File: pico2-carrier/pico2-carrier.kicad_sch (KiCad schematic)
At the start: 27 parts, among them IC1 TFDU4101-TT3, IC2 M95512-DWDW4TP_K, IC3 W25Q128JVSIM_TR, SW1 RUN, SW2 BUT_L, SW3 BUT_M, SW4 BUT_R, U1 Pico 2

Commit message: start work on PCB
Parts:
- IC1: footprint TFDU4101-TR3 -> SamacsysParts:TFDU4101-TR3
- IC2: footprint SOP65P640X120-8N -> SamacsysParts:SOP65P640X120-8N
- IC3: footprint SOIC127P790X216-8N -> SamacsysParts:SOIC127P790X216-8N
- R3: footprint (none) -> Resistor_SMD:R_0402_1005Metric
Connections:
- net ACCEL_INT1: now also U1.11 (GPIO8); no longer U1.10 (GPIO7)
- net BUT_L: now also U1.25 (GPIO19); no longer U1.29 (GPIO22)
- net BUT_M: now also U1.29 (GPIO22); no longer U1.31 (GPIO26_ADC0)
- net BUT_R: now also U1.31 (GPIO26_ADC0); no longer U1.32 (GPIO27_ADC1)
- net ~{ACCEL_CSB}: now also U1.10 (GPIO7); no longer U1.9 (GPIO6)
- net ~{BAT_CE}: now also U1.32 (GPIO27_ADC1); no longer U1.34 (GPIO28_ADC2)
- net ~{BAT_INT}: now also U1.34 (GPIO28_ADC2); no longer U1.25 (GPIO19)
- net ~{FLASH_CSB}: now also U1.9 (GPIO6); no longer U1.11 (GPIO8)
- net VSYS_IN: now reaches JP2.1 (A), U1.39 (VSYS)
- net 3V3_OUT: now reaches JP3.1 (A), U1.35 (ADC_VREF), U1.36 (3V3)
- net VBUS_OUT: now reaches JP1.1 (A), U1.40 (VBUS)
- no-connect marks 4 -> 5
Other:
- note added: "Ceramic"
- note added: "Current lim = 60mA"
- note added: "Tantalum/fast rise"
- moved on the sheet: JP1, JP2

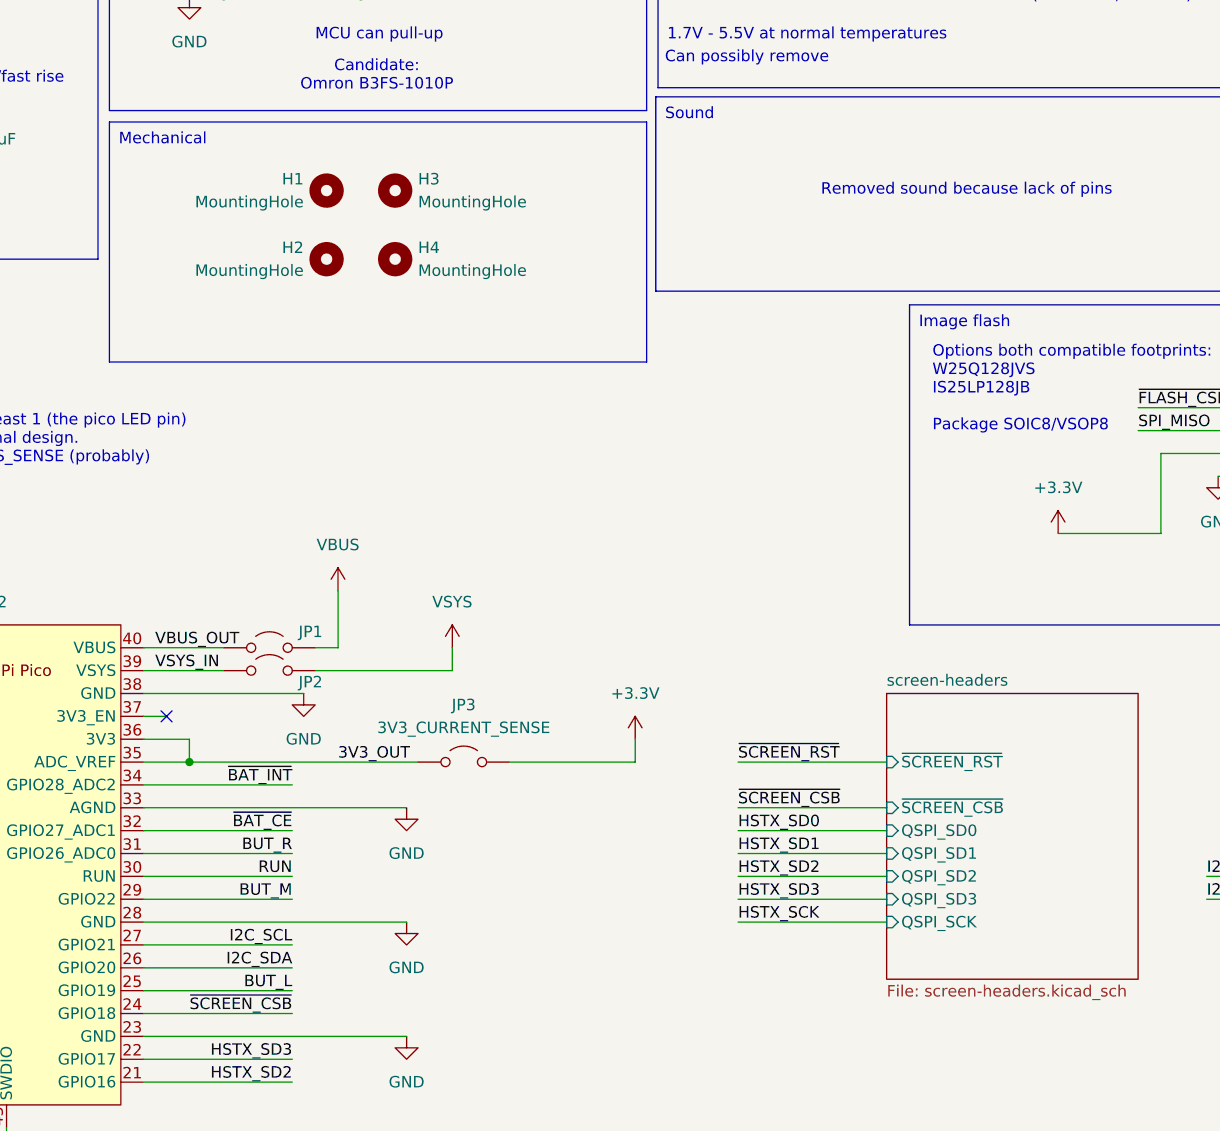
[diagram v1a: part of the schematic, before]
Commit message: finish routing - DRC ok
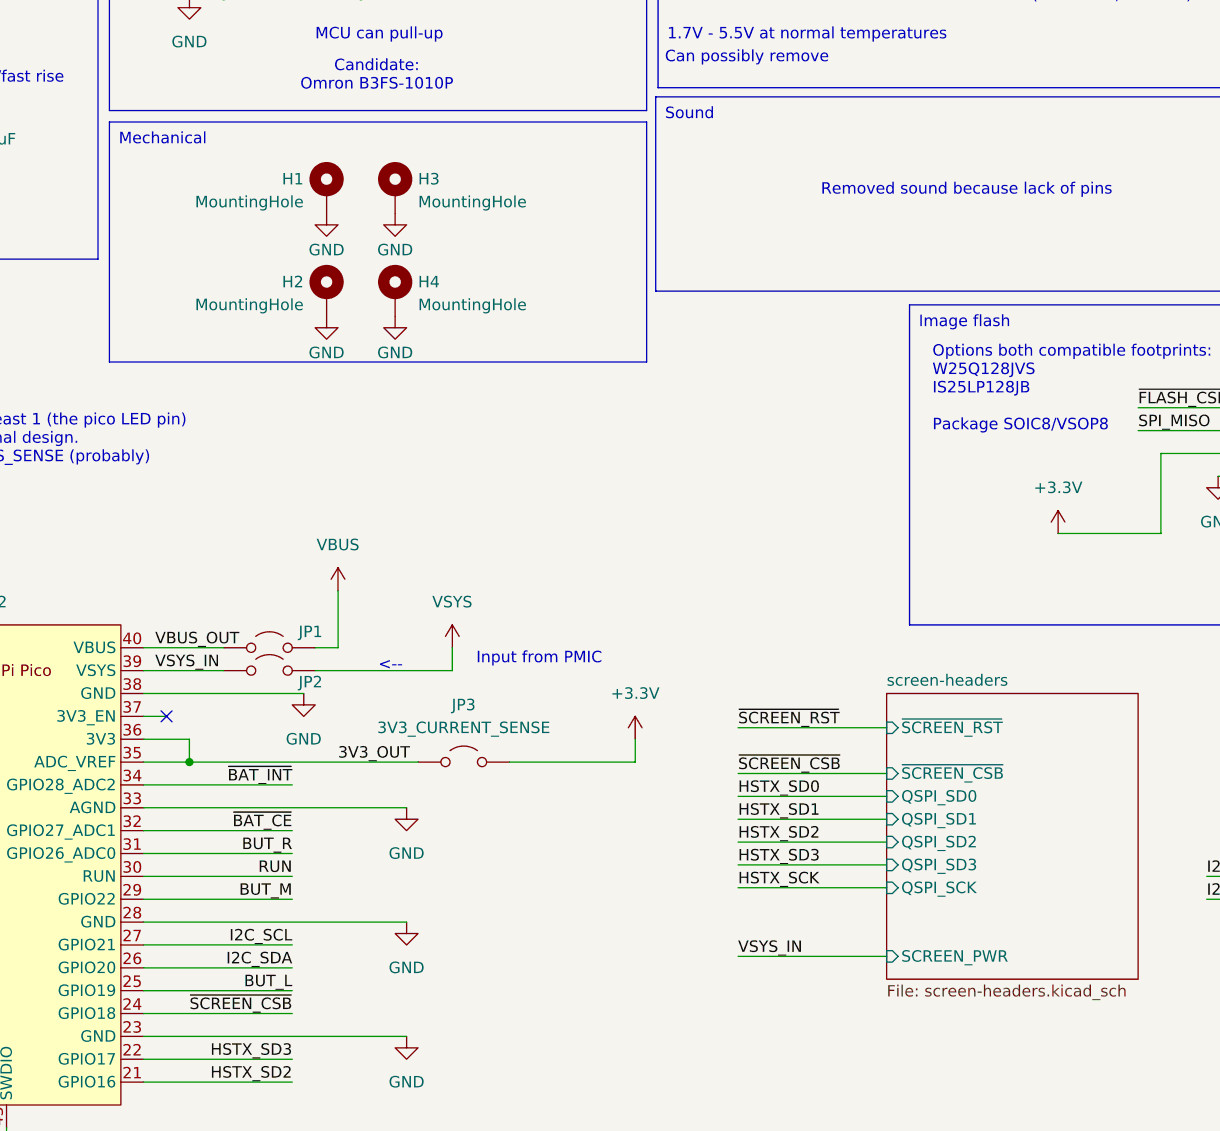
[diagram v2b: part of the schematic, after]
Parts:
- H1, H2, H3, H4: symbol Mechanical:MountingHole -> Mechanical:MountingHole_Pad
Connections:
- net GND: now also H1.1, H2.1, H3.1, H4.1
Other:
- sheet screen-headers ports: added SCREEN_PWR; removed none
- note added: "<--"
- note added: "Input from PMIC"

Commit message: pcb tweaks
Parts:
- H1, H2, H3, H4: footprint MountingHole:MountingHole_2.2mm_M2 -> MountingHole:MountingHole_2.2mm_M2_DIN965_Pad_TopBottom
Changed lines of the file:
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@@
 			)
 		)
-		(property "Footprint" "MountingHole:MountingHole_2.2mm_M2"
+		(property "Footprint" "MountingHole:MountingHole_2.2mm_M2_DIN965_Pad_TopBottom"
 			(at 115.57 76.2 0)
 			(effects
@@
 			)
 		)
-		(property "Footprint" "MountingHole:MountingHole_2.2mm_M2"
+		(property "Footprint" "MountingHole:MountingHole_2.2mm_M2_DIN965_Pad_TopBottom"
 			(at 107.95 64.77 0)
 			(effects
@@
 			)
 		)
-		(property "Footprint" "MountingHole:MountingHole_2.2mm_M2"
+		(property "Footprint" "MountingHole:MountingHole_2.2mm_M2_DIN965_Pad_TopBottom"
 			(at 107.95 76.2 0)
 			(effects
@@
 			)
 		)
-		(property "Footprint" "MountingHole:MountingHole_2.2mm_M2"
+		(property "Footprint" "MountingHole:MountingHole_2.2mm_M2_DIN965_Pad_TopBottom"
 			(at 115.57 64.77 0)
 			(effects

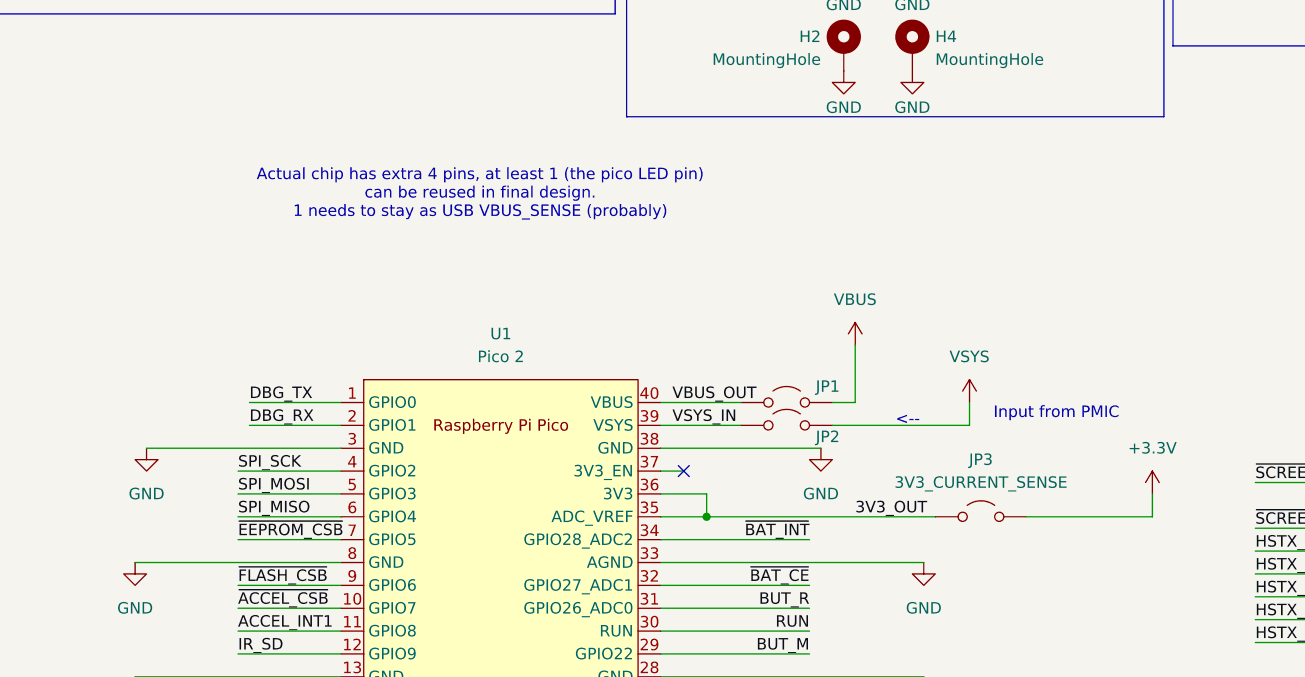
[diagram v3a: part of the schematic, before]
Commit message: add PFET to VSYS input
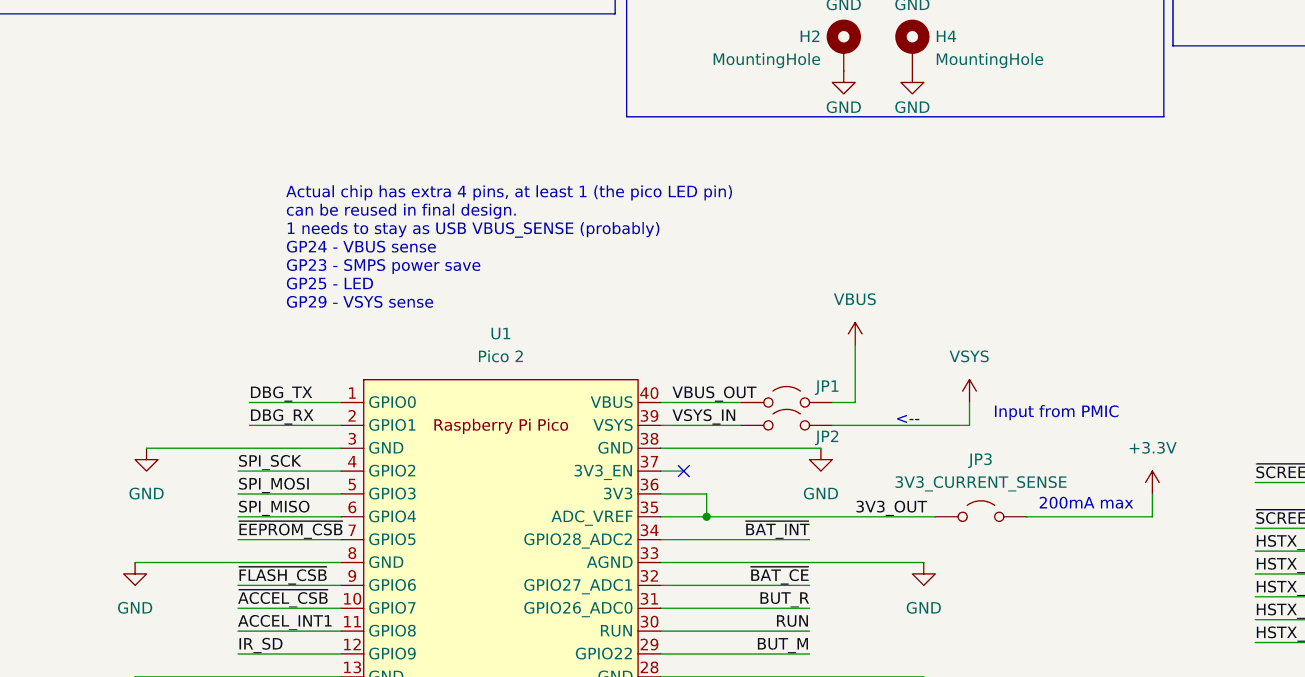
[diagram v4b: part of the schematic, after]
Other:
- note added: "200mA max"
- note added: "Actual chip has extra 4 pins, at least 1 (the pico LED pin) can be reused in final design. 1 needs to stay as USB VBUS_SENSE (probably) GP24 - VBUS sense GP23 - SMPS power save GP25 - LED GP29 - VSYS sense"
- note removed: "Actual chip has extra 4 pins, at least 1 (the pico LED pin) can be reused in final design. 1 needs to stay as USB VBUS_SENSE (probably)"
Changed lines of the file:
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@@
+		)
+	)
+	(text "200mA max"
+		(exclude_from_sim no)
+		(at 134.874 127 0)
+		(effects
+			(font
+				(size 1.27 1.27)
+			)
 		)
 	)
@@
 		)
 	)
-	(text "Actual chip has extra 4 pins, at least 1 (the pico LED pin)\ncan be reused in final design.\n1 needs to stay as USB VBUS_SENSE (probably)"
+	(text "Actual chip has extra 4 pins, at least 1 (the pico LED pin)\ncan be reused in final design.\n1 needs to stay as USB VBUS_SENSE (probably)\nGP24 - VBUS sense\nGP23 - SMPS power save\nGP25 - LED\nGP29 - VSYS sense"
 		(exclude_from_sim no)
-		(at 67.564 92.456 0)
+		(at 45.974 98.552 0)
 		(effects
 			(font
 				(size 1.27 1.27)
 			)
+			(justify left)
 		)
 	)

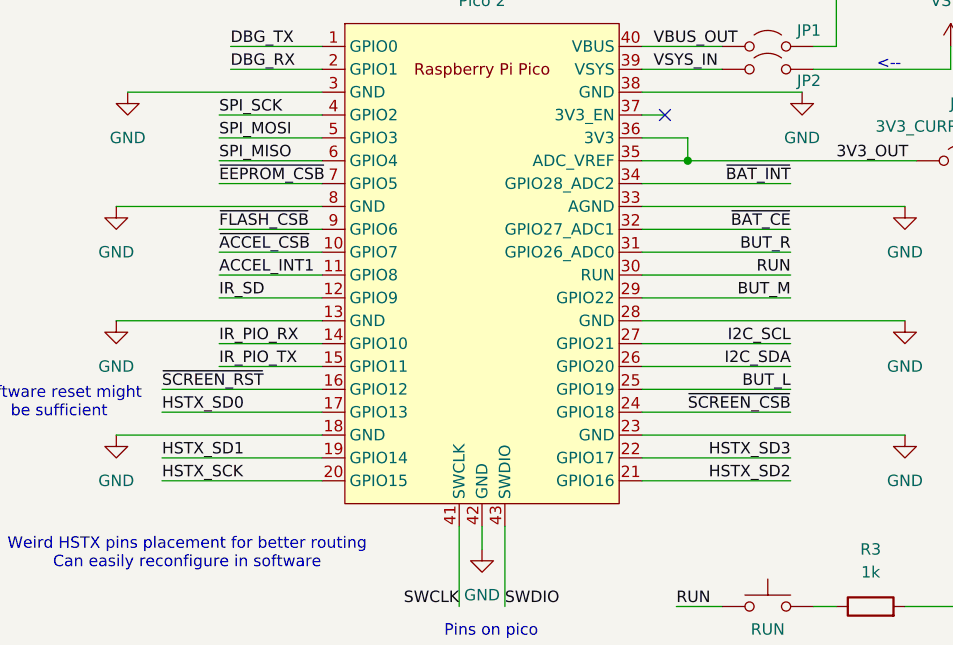
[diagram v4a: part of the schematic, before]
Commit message: carrier: new pcb degisn for better screen placement
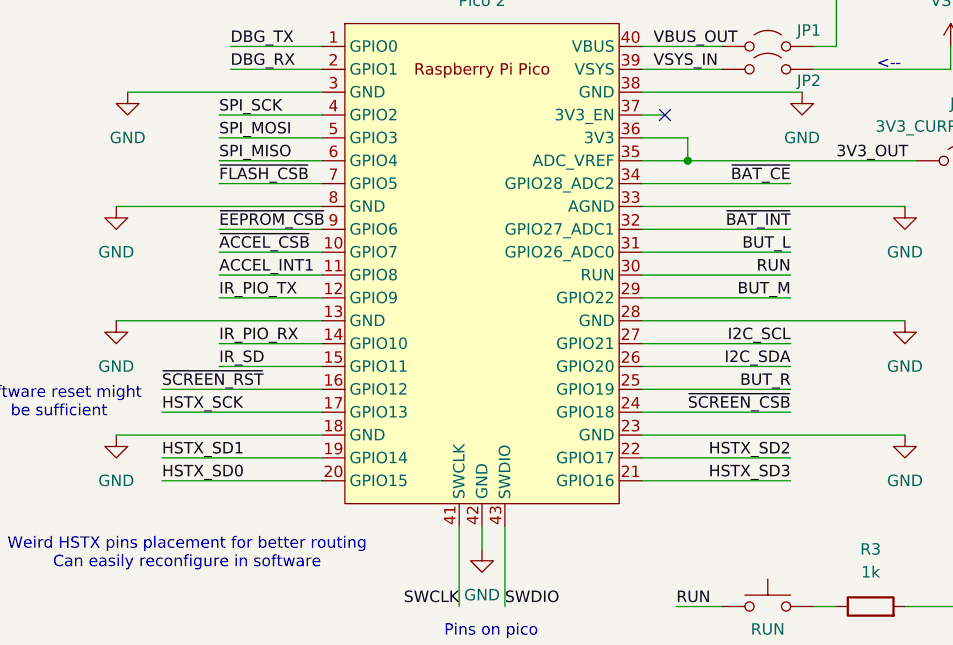
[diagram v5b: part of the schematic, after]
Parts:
- JP1: value Jumper_2_Open -> VBUS_SENSE
- JP2: value Jumper_2_Open -> VSYS_SENSE
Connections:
- net BUT_L: now also U1.31 (GPIO26_ADC0); no longer U1.25 (GPIO19)
- net BUT_R: now also U1.25 (GPIO19); no longer U1.31 (GPIO26_ADC0)
- net HSTX_SCK: now also U1.17 (GPIO13); no longer U1.20 (GPIO15)
- net HSTX_SD0: now also U1.20 (GPIO15); no longer U1.17 (GPIO13)
- net HSTX_SD2: now also U1.22 (GPIO17); no longer U1.21 (GPIO16)
- net HSTX_SD3: now also U1.21 (GPIO16); no longer U1.22 (GPIO17)
- net IR_PIO_TX: now also U1.12 (GPIO9); no longer U1.15 (GPIO11)
- net IR_SD: now also U1.15 (GPIO11); no longer U1.12 (GPIO9)
- net ~{BAT_CE}: now also U1.34 (GPIO28_ADC2); no longer U1.32 (GPIO27_ADC1)
- net ~{BAT_INT}: now also U1.32 (GPIO27_ADC1); no longer U1.34 (GPIO28_ADC2)
- net ~{EEPROM_CSB}: now also U1.9 (GPIO6); no longer U1.7 (GPIO5)
- net ~{FLASH_CSB}: now also U1.7 (GPIO5); no longer U1.9 (GPIO6)
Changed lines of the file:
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@@
 		)
 	)
-	(label "HSTX_SD2"
-		(at 104.14 163.83 180)
-		(fields_autoplaced yes)
-		(effects
-			(font
-				(size 1.27 1.27)
-			)
-			(justify right bottom)
-		)
-	)
 	(label "SPI_MISO"
 		(at 40.64 128.27 0)
@@
 		)
 	)
-	(label "~{FLASH_CSB}"
-		(at 40.64 135.89 0)
+	(label "RUN"
+		(at 104.14 140.97 180)
 		(fields_autoplaced yes)
 		(effects
@@
 				(size 1.27 1.27)
 			)
-			(justify left bottom)
+			(justify right bottom)
 		)
 	)
-	(label "RUN"
-		(at 104.14 140.97 180)
+	(label "I2C_SCL"
+		(at 205.74 140.97 0)
 		(fields_autoplaced yes)
 		(effects
@@
 				(size 1.27 1.27)
 			)
-			(justify right bottom)
+			(justify left bottom)
 		)
 	)
-	(label "I2C_SCL"
-		(at 205.74 140.97 0)
+	(label "IR_PIO_TX"
+		(at 40.64 143.51 0)
 		(fields_autoplaced yes)
 		(effects
@@
 		)
 	)
-	(label "IR_PIO_TX"
-		(at 40.64 151.13 0)
+	(label "BUT_L"
+		(at 104.14 138.43 180)
 		(fields_autoplaced yes)
 		(effects
@@
 				(size 1.27 1.27)
 			)
-			(justify left bottom)
+			(justify right bottom)
 		)
 	)
@@
 		)
 	)
-	(label "HSTX_SD3"
-		(at 104.14 161.29 180)
-		(fields_autoplaced yes)
-		(effects
-			(font
-				(size 1.27 1.27)
-			)
-			(justify right bottom)
-		)
-	)
 	(label "SPI_SCK"
 		(at 275.59 93.98 180)
@@
 		)
 	)
-	(label "~{SCREEN_RST}"
-		(at 34.29 153.67 0)
+	(label "BUT_R"
+		(at 104.14 153.67 180)
 		(fields_autoplaced yes)
 		(effects
@@
 				(size 1.27 1.27)
 			)
-			(justify left bottom)
+			(justify right bottom)
 		)
 	)
-	(label "SPI_MISO"
-		(at 198.12 91.44 0)
+	(label "~{SCREEN_RST}"
+		(at 34.29 153.67 0)
 		(fields_autoplaced yes)
 		(effects
@@
 		)
 	)
-	(label "I2C_SDA"
-		(at 205.74 143.51 0)
+	(label "SPI_MISO"
+		(at 198.12 91.44 0)
 		(fields_autoplaced yes)
 		(effects
@@
 		)
 	)
-	(label "~{SCREEN_CSB}"
-		(at 104.14 156.21 180)
+	(label "IR_SD"
+		(at 40.64 151.13 0)
 		(fields_autoplaced yes)
 		(effects
@@
 				(size 1.27 1.27)
 			)
-			(justify right bottom)
+			(justify left bottom)
 		)
 	)
-	(label "BUT_R"
-		(at 104.14 138.43 180)
+	(label "I2C_SDA"
+		(at 205.74 143.51 0)
 		(fields_autoplaced yes)
 		(effects
@@
 				(size 1.27 1.27)
 			)
-			(justify right bottom)
+			(justify left bottom)
 		)
 	)
-	(label "~{BAT_INT}"
-		(at 104.14 130.81 180)
+	(label "~{SCREEN_CSB}"
+		(at 104.14 156.21 180)
 		(fields_autoplaced yes)
 		(effects
@@
 		)
 	)
-	(label "HSTX_SD0"
-		(at 34.29 156.21 0)
+	(label "DBG_TX"
+		(at 41.91 115.57 0)
 		(fields_autoplaced yes)
 		(effects
@@
 		)
 	)
-	(label "DBG_TX"
-		(at 41.91 115.57 0)
+	(label "SPI_MISO"
+		(at 152.4 25.4 0)
 		(fields_autoplaced yes)
 		(effects
@@
 		)
 	)
-	(label "SPI_MISO"
-		(at 152.4 25.4 0)
+	(label "~{FLASH_CSB}"
+		(at 40.64 130.81 0)
 		(fields_autoplaced yes)
 		(effects
@@
 		)
 	)
-	(label "HSTX_SD1"
-		(at 34.29 161.29 0)
+	(label "HSTX_SD2"
+		(at 104.14 161.29 180)
 		(fields_autoplaced yes)
 		(effects
@@
 				(size 1.27 1.27)
 			)
-			(justify left bottom)
+			(justify right bottom)
 		)
 	)
@@
 		)
 	)
-	(label "~{EEPROM_CSB}"
-		(at 40.64 130.81 0)
-		(fields_autoplaced yes)
-		(effects
-			(font
-				(size 1.27 1.27)
-			)
-			(justify left bottom)
-		)
-	)
 	(label "HSTX_SCK"
 		(at 153.67 142.24 0)
@@
 		)
 	)
-	(label "~{FLASH_CSB}"
-		(at 198.12 88.9 0)
+	(label "HSTX_SD0"
+		(at 34.29 163.83 0)
 		(fields_autoplaced yes)
 		(effects
@@
 		)
 	)
-	(label "SPI_MOSI"
-		(at 40.64 125.73 0)
+	(label "~{FLASH_CSB}"
+		(at 198.12 88.9 0)
 		(fields_autoplaced yes)
 		(effects
@@
 		)
 	)
-	(label "BUT_L"
-		(at 104.14 153.67 180)
+	(label "SPI_MOSI"
+		(at 40.64 125.73 0)
 		(fields_autoplaced yes)
 		(effects
@@
 				(size 1.27 1.27)
 			)
-			(justify right bottom)
+			(justify left bottom)
 		)
 	)
@@
 		)
 	)
-	(label "IR_SD"
-		(at 40.64 143.51 0)
+	(label "~{BAT_CE}"
+		(at 104.14 130.81 180)
 		(fields_autoplaced yes)
 		(effects
@@
 				(size 1.27 1.27)
 			)
-			(justify left bottom)
+			(justify right bottom)
 		)
 	)
@@
 		)
 	)
-	(label "HSTX_SCK"
-		(at 34.29 163.83 0)
+	(label "~{EEPROM_CSB}"
+		(at 40.64 135.89 0)
+		(fields_autoplaced yes)
+		(effects
+			(font
+				(size 1.27 1.27)
+			)
+			(justify left bottom)
+		)
+	)
+	(label "HSTX_SD1"
+		(at 34.29 161.29 0)
 		(fields_autoplaced yes)
 		(effects
@@
 		)
 	)
-	(label "~{BAT_CE}"
-		(at 104.14 135.89 180)
+	(label "~{BAT_INT}"
+		(at 215.9 152.4 0)
 		(fields_autoplaced yes)
 		(effects
@@
 				(size 1.27 1.27)
 			)
-			(justify right bottom)
+			(justify left bottom)
 		)
 	)
-	(label "~{BAT_INT}"
-		(at 215.9 152.4 0)
+	(label "HSTX_SCK"
+		(at 34.29 156.21 0)
 		(fields_autoplaced yes)
 		(effects
@@
 		)
 	)
+	(label "HSTX_SD3"
+		(at 104.14 163.83 180)
+		(fields_autoplaced yes)
+		(effects
+			(font
+				(size 1.27 1.27)
+			)
+			(justify right bottom)
+		)
+	)
 	(label "SPI_MOSI"
 		(at 229.87 38.1 0)
@@
 		)
 	)
+	(label "~{BAT_INT}"
+		(at 104.14 135.89 180)
+		(fields_autoplaced yes)
+		(effects
+			(font
+				(size 1.27 1.27)
+			)
+			(justify right bottom)
+		)
+	)
 	(symbol
 		(lib_id "power:GND")
@@
 			)
 		)
-		(property "Value" "Jumper_2_Open"
+		(property "Value" "VSYS_SENSE"
 			(at 101.6 114.3 0)
 			(effects
@@
 			)
 		)
-		(property "Value" "Jumper_2_Open"
+		(property "Value" "VBUS_SENSE"
 			(at 101.6 111.76 0)
 			(effects
